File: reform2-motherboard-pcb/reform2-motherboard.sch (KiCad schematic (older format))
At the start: 45 parts, among them J15 Conn_01x33, J18 Conn_01x03_Male, J19 JTAG, J20 Conn_01x03_Male, SW3 SW_DIP_x01, SW5 SW_DIP_x04, SW6 SW_Push, U1 Nitrogen8M

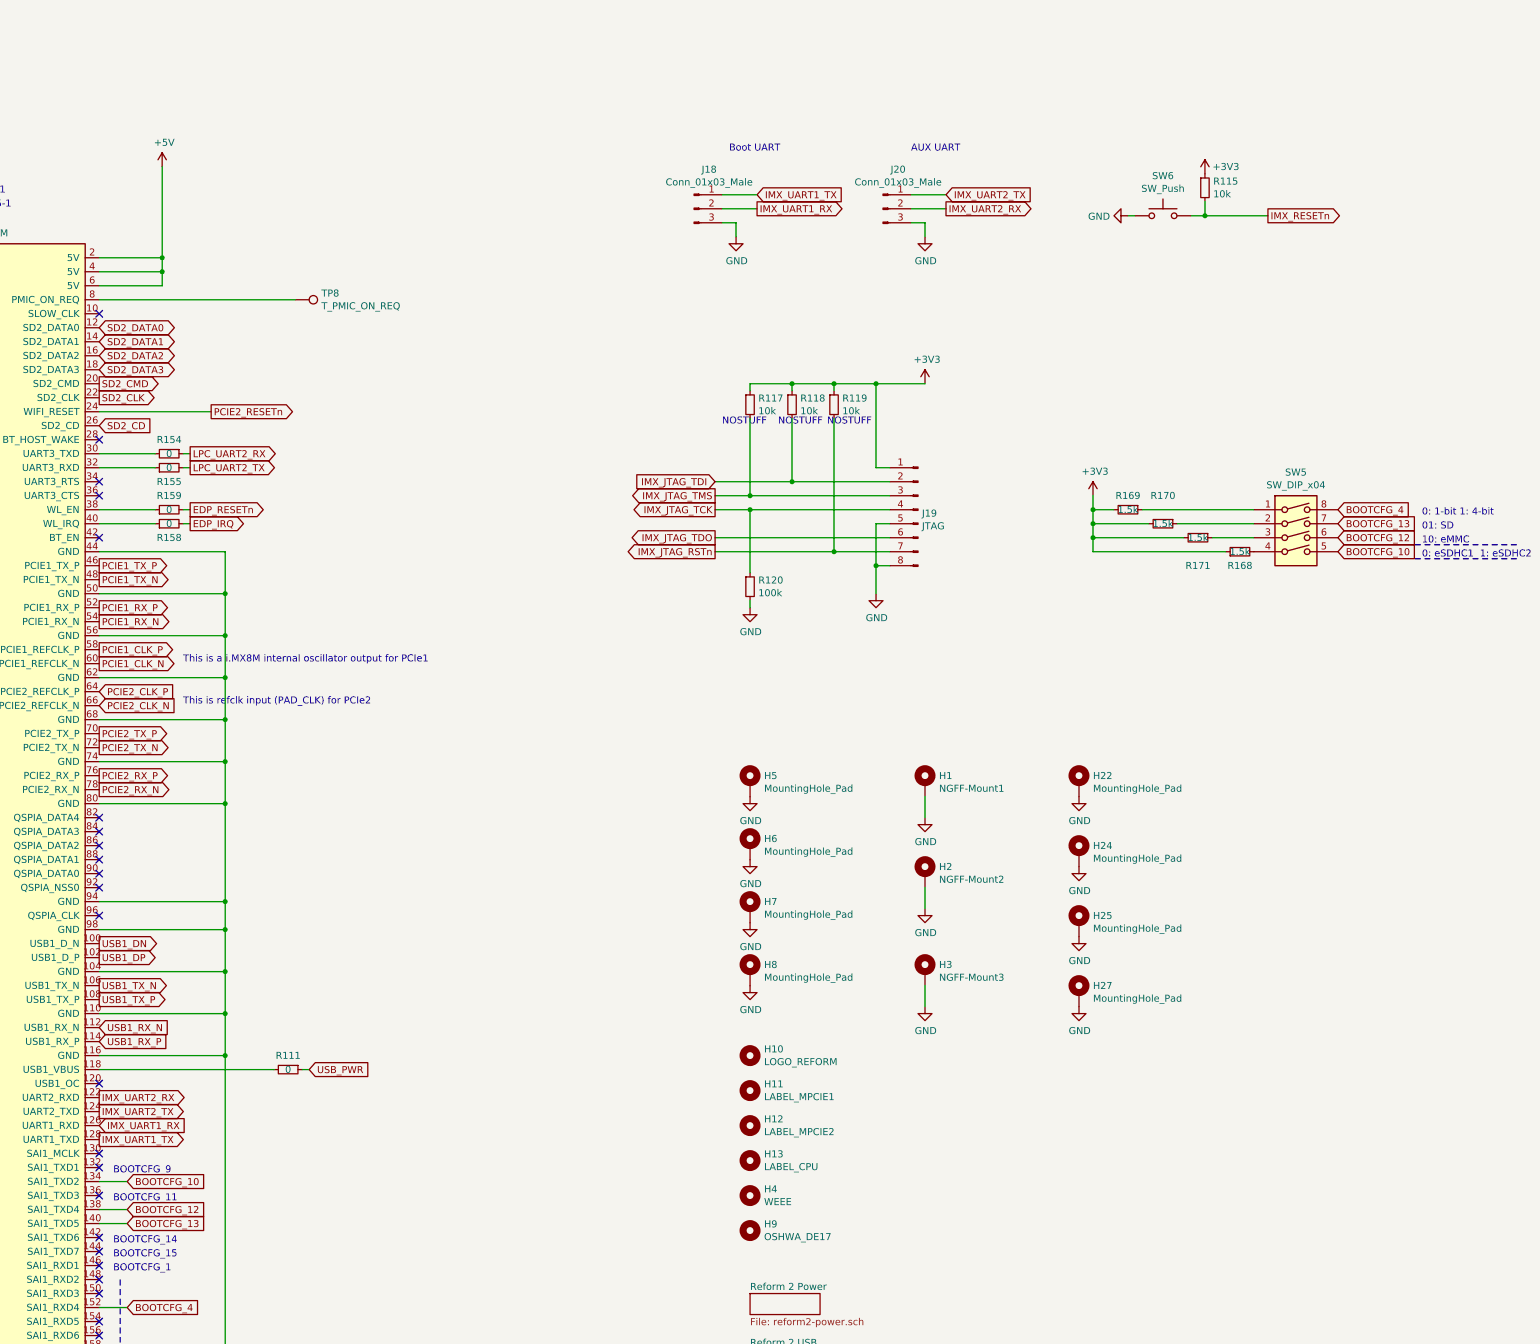
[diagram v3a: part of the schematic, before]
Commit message: reform2-motherboard: first R-1 snapshot. main changes: EMI, ESD, audio filter, enable FETs, SHDN fix, more rail switches
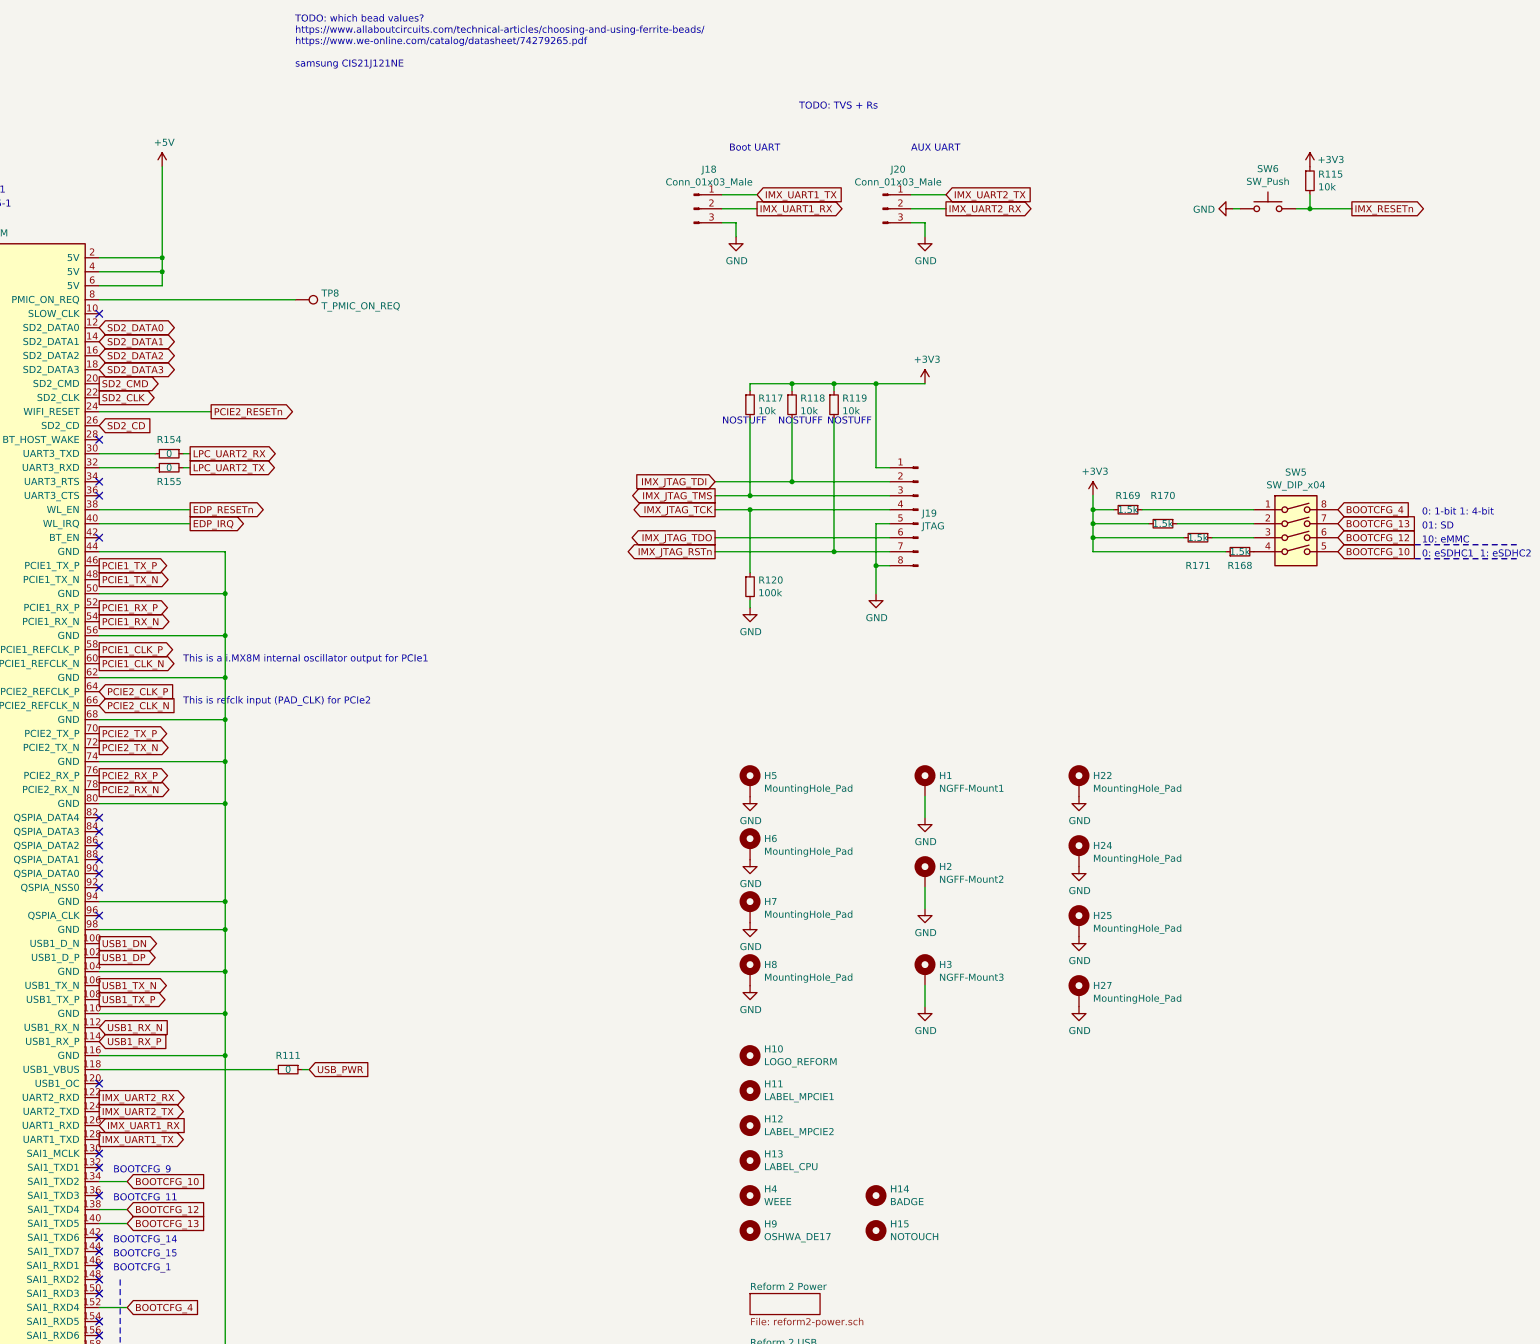
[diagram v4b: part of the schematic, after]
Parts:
- removed R158, R159: 0, Resistor_SMD:R_0603_1608Metric, symbol Device:R_Small
- added H14: BADGE, footprints:reform2-motherboard-badge, symbol Mechanical:MountingHole
- added H15: NOTOUCH, Symbol:ESD-Logo_8.9x8mm_SilkScreen, symbol Mechanical:MountingHole
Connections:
- net EDP_IRQ: now also U1.40 (WL_IRQ)
- net EDP_RESETn: now also U1.38 (WL_EN)
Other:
- note added: "TODO: TVS + Rs"
- note added: "TODO: which bead values?\nhttps://www.allaboutcircuits.com/technical-articles/choosing-and-using-ferrite-beads/\nhttps://www.we-online.com/catalog/datasheet/74279265.pdf\n\nsamsung CIS21J121NE"
- moved on the sheet: R115, SW6
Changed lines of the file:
@@
 Comment4 ""
 $EndDescr
-Wire Wire Line
-	10400 5350 10800 5350
-Wire Wire Line
-	11050 5350 11000 5350
 Text GLabel 11050 5350 2    50   Output ~ 0
 EDP_RESETn
-$Comp
-L Device:R_Small R159
-U 1 1 63FE6619
-P 10900 5350
-F 0 "R159" V 11000 5350 50  0000 C CNN
-F 1 "0" V 10900 5350 50  0000 C CNN
-F 2 "Resistor_SMD:R_0603_1608Metric" H 10900 5350 50  0001 C CNN
-F 3 "~" H 10900 5350 50  0001 C CNN
-F 4 "Vishay Dale" H 10900 5350 50  0001 C CNN "Manufacturer"
-F 5 "CRCW06030000Z0EAC" H 10900 5350 50  0001 C CNN "Manufacturer_No"
-F 6 "Mouser" H 10900 5350 50  0001 C CNN "Distributor"
-F 7 "y" H 10900 5350 50  0001 C CNN "Checked"
-	1    10900 5350
-	0    -1   -1   0
-$EndComp
-Wire Wire Line
-	10400 5450 10800 5450
-Wire Wire Line
-	11050 5450 11000 5450
-$Comp
-L Device:R_Small R158
-U 1 1 636E4DF1
-P 10900 5450
-F 0 "R158" V 10800 5450 50  0000 C CNN
-F 1 "0" V 10900 5450 50  0000 C CNN
-F 2 "Resistor_SMD:R_0603_1608Metric" H 10900 5450 50  0001 C CNN
-F 3 "~" H 10900 5450 50  0001 C CNN
-F 4 "Vishay Dale" H 10900 5450 50  0001 C CNN "Manufacturer"
-F 5 "CRCW06030000Z0EAC" H 10900 5450 50  0001 C CNN "Manufacturer_No"
-F 6 "Mouser" H 10900 5450 50  0001 C CNN "Distributor"
-F 7 "y" H 10900 5450 50  0001 C CNN "Checked"
-	1    10900 5450
-	0    -1   -1   0
-$EndComp
 Text GLabel 11050 5450 2    50   Output ~ 0
 EDP_IRQ
@@
 Text GLabel 8700 7850 0    50   Input ~ 0
 IMX_RESETn
-Text GLabel 18750 3250 2    50   Output ~ 0
+Text GLabel 19350 3200 2    50   Output ~ 0
 IMX_RESETn
 $Comp
@@
 L Device:R_Small R115
 U 1 1 5DC1194C
-P 18300 3050
-F 0 "R115" H 18359 3096 50  0000 L CNN
-F 1 "10k" H 18359 3005 50  0000 L CNN
-F 2 "Resistor_SMD:R_0603_1608Metric" H 18300 3050 50  0001 C CNN
-F 3 "~" H 18300 3050 50  0001 C CNN
-F 4 "Yageo" H 18300 3050 50  0001 C CNN "Manufacturer"
-F 5 "RC0603FR-0710KL" H 18300 3050 50  0001 C CNN "Manufacturer_No"
-F 6 "y" H 18300 3050 50  0001 C CNN "Checked"
-F 7 "Mouser" H 18300 3050 50  0001 C CNN "Distributor"
-	1    18300 3050
+P 19050 3000
+F 0 "R115" H 19109 3046 50  0000 L CNN
+F 1 "10k" H 19109 2955 50  0000 L CNN
+F 2 "Resistor_SMD:R_0603_1608Metric" H 19050 3000 50  0001 C CNN
+F 3 "~" H 19050 3000 50  0001 C CNN
+F 4 "Yageo" H 19050 3000 50  0001 C CNN "Manufacturer"
+F 5 "RC0603FR-0710KL" H 19050 3000 50  0001 C CNN "Manufacturer_No"
+F 6 "y" H 19050 3000 50  0001 C CNN "Checked"
+F 7 "Mouser" H 19050 3000 50  0001 C CNN "Distributor"
+	1    19050 3000
 	1    0    0    -1
 $EndComp
@@
 L power:+3V3 #PWR059
 U 1 1 5DC110DB
-P 18300 2950
-F 0 "#PWR059" H 18300 2800 50  0001 C CNN
-F 1 "+3V3" H 18450 3000 50  0000 C CNN
-F 2 "" H 18300 2950 50  0001 C CNN
-F 3 "" H 18300 2950 50  0001 C CNN
-	1    18300 2950
-	1    0    0    -1
-$EndComp
-Wire Wire Line
-	17750 3250 17800 3250
+P 19050 2900
+F 0 "#PWR059" H 19050 2750 50  0001 C CNN
+F 1 "+3V3" H 19200 2950 50  0000 C CNN
+F 2 "" H 19050 2900 50  0001 C CNN
+F 3 "" H 19050 2900 50  0001 C CNN
+	1    19050 2900
+	1    0    0    -1
+$EndComp
+Wire Wire Line
+	18500 3200 18550 3200
 $Comp
 L power:GND #PWR054
 U 1 1 5DBFED7E
-P 17750 3250
-F 0 "#PWR054" H 17750 3000 50  0001 C CNN
-F 1 "GND" V 17755 3122 50  0000 R CNN
-F 2 "" H 17750 3250 50  0001 C CNN
-F 3 "" H 17750 3250 50  0001 C CNN
-	1    17750 3250
+P 18500 3200
+F 0 "#PWR054" H 18500 2950 50  0001 C CNN
+F 1 "GND" V 18505 3072 50  0000 R CNN
+F 2 "" H 18500 3200 50  0001 C CNN
+F 3 "" H 18500 3200 50  0001 C CNN
+	1    18500 3200
 	0    1    1    0
 $EndComp
@@
 L Switch:SW_Push SW?
 U 1 1 5DBC8BEC
-P 18000 3250
+P 18750 3200
 AR Path="/5CC81028/5DBC8BEC" Ref="SW?"  Part="1"
 AR Path="/5DBC8BEC" Ref="SW6"  Part="1"
-F 0 "SW6" H 18000 3535 50  0000 C CNN
-F 1 "SW_Push" H 18000 3444 50  0000 C CNN
-F 2 "Button_Switch_SMD:SW_Push_1P1T_NO_CK_KMR2" H 18000 3450 50  0001 C CNN
-F 3 "~" H 18000 3450 50  0001 C CNN
-F 4 "C&K" H 18000 3250 50  0001 C CNN "Manufacturer"
-F 5 "KMR221GLFS" H 18000 3250 50  0001 C CNN "Manufacturer_No"
-F 6 "y" H 18000 3250 50  0001 C CNN "Checked"
-F 7 "Mouser" H 18000 3250 50  0001 C CNN "Distributor"
-	1    18000 3250
+F 0 "SW6" H 18750 3485 50  0000 C CNN
+F 1 "SW_Push" H 18750 3394 50  0000 C CNN
+F 2 "Button_Switch_SMD:SW_Push_1P1T_NO_CK_KMR2" H 18750 3400 50  0001 C CNN
+F 3 "~" H 18750 3400 50  0001 C CNN
+F 4 "C&K" H 18750 3200 50  0001 C CNN "Manufacturer"
+F 5 "KMR221GLFS" H 18750 3200 50  0001 C CNN "Manufacturer_No"
+F 6 "y" H 18750 3200 50  0001 C CNN "Checked"
+F 7 "Mouser" H 18750 3200 50  0001 C CNN "Distributor"
+	1    18750 3200
 	1    0    0    -1
 $EndComp
@@
 	8700 10550 7300 10550
 Wire Wire Line
-	18200 3250 18300 3250
-Wire Wire Line
-	18300 3150 18300 3250
-Connection ~ 18300 3250
-Wire Wire Line
-	18300 3250 18750 3250
+	18950 3200 19050 3200
+Wire Wire Line
+	19050 3100 19050 3200
+Connection ~ 19050 3200
+Wire Wire Line
+	19050 3200 19350 3200
 Wire Wire Line
 	6600 5350 8700 5350
@@
 $EndComp
 NoConn ~ 8700 5450
+Wire Wire Line
+	10400 5350 11050 5350
+Wire Wire Line
+	10400 5450 11050 5450
+Text Notes 11800 2200 0    50   ~ 0
+TODO: which bead values?\nhttps://www.allaboutcircuits.com/technical-articles/choosing-and-using-ferrite-beads/\nhttps://www.we-online.com/catalog/datasheet/74279265.pdf\n\nsamsung CIS21J121NE
+Text Notes 15400 2500 0    50   ~ 0
+TODO: TVS + Rs
+$Comp
+L Mechanical:MountingHole H14
+U 1 1 64382D78
+P 15950 10250
+F 0 "H14" H 16050 10296 50  0000 L CNN
+F 1 "BADGE" H 16050 10205 50  0000 L CNN
+F 2 "footprints:reform2-motherboard-badge" H 15950 10250 50  0001 C CNN
+F 3 "~" H 15950 10250 50  0001 C CNN
+F 4 "y" H 15950 10250 50  0001 C CNN "Checked"
+F 5 "None" H 15950 10250 50  0001 C CNN "Distributor"
+F 6 "y" H 15950 10250 50  0001 C CNN "DNP"
+	1    15950 10250
+	1    0    0    -1
+$EndComp
+$Comp
+L Mechanical:MountingHole H15
+U 1 1 64785954
+P 15950 10500
+F 0 "H15" H 16050 10546 50  0000 L CNN
+F 1 "NOTOUCH" H 16050 10455 50  0000 L CNN
+F 2 "Symbol:ESD-Logo_8.9x8mm_SilkScreen" H 15950 10500 50  0001 C CNN
+F 3 "~" H 15950 10500 50  0001 C CNN
+F 4 "y" H 15950 10500 50  0001 C CNN "Checked"
+F 5 "None" H 15950 10500 50  0001 C CNN "Distributor"
+F 6 "y" H 15950 10500 50  0001 C CNN "DNP"
+	1    15950 10500
+	1    0    0    -1
+$EndComp
 $EndSCHEMATC

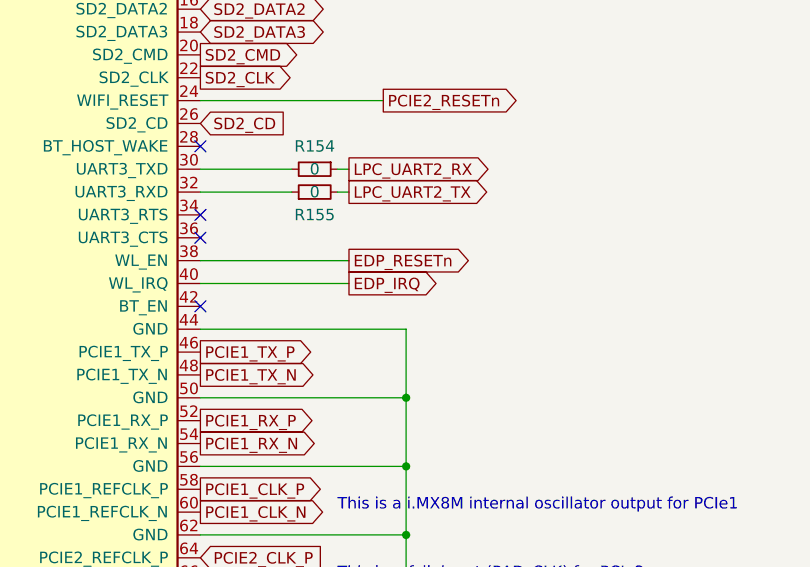
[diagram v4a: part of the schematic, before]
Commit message: reform2-motherboard: R-1 silkscreen cleanup; usb hub reset pulldown added
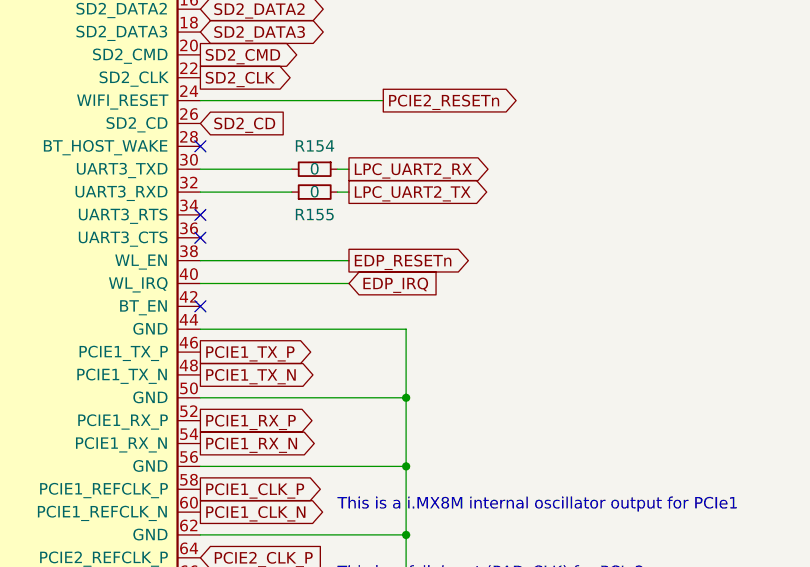
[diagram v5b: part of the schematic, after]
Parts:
- J18: footprint Connector_PinHeader_2.54mm:PinHeader_1x03_P2.54mm_Vertical -> Connector_PinHeader_2.54mm:PinHeader_1x03_P2.54mm_Horizontal
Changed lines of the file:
@@
 Text GLabel 11050 5350 2    50   Output ~ 0
 EDP_RESETn
-Text GLabel 11050 5450 2    50   Output ~ 0
+Text GLabel 11050 5450 2    50   Input ~ 0
 EDP_IRQ
 Text GLabel 8700 7250 0    50   Input ~ 0
@@
 F 0 "J18" H 14758 3481 50  0000 C CNN
 F 1 "Conn_01x03_Male" H 14758 3390 50  0000 C CNN
-F 2 "Connector_PinHeader_2.54mm:PinHeader_1x03_P2.54mm_Vertical" H 14650 3200 50  0001 C CNN
+F 2 "Connector_PinHeader_2.54mm:PinHeader_1x03_P2.54mm_Horizontal" H 14650 3200 50  0001 C CNN
 F 3 "~" H 14650 3200 50  0001 C CNN
 F 4 "Wurth" H 14650 3200 50  0001 C CNN "Manufacturer"

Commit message: motherboard: r-1 release snapshot
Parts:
- removed H4: WEEE, Symbol:WEEE-Logo_4.2x6mm_SilkScreen, symbol Mechanical:MountingHole
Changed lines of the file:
@@
 Sheet 1 9
 Title "MNT Reform 2"
-Date "2020-05-19"
-Rev "2.0D-4"
+Date "2020-09-24"
+Rev "2.0R-1"
 Comp "MNT Research GmbH"
 Comment1 "https://mntre.com"
@@
 	1    0    0    -1
 $EndComp
-$Comp
-L Mechanical:MountingHole H4
-U 1 1 5D3EF97D
-P 15050 10250
-F 0 "H4" H 15150 10296 50  0000 L CNN
-F 1 "WEEE" H 15150 10205 50  0000 L CNN
-F 2 "Symbol:WEEE-Logo_4.2x6mm_SilkScreen" H 15050 10250 50  0001 C CNN
-F 3 "~" H 15050 10250 50  0001 C CNN
-F 4 "y" H 15050 10250 50  0001 C CNN "Checked"
-F 5 "None" H 15050 10250 50  0001 C CNN "Distributor"
-F 6 "y" H 15050 10250 50  0001 C CNN "DNP"
-	1    15050 10250
-	1    0    0    -1
-$EndComp
